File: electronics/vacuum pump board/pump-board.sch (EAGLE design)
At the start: 6 parts, among them J1 JST-PH3

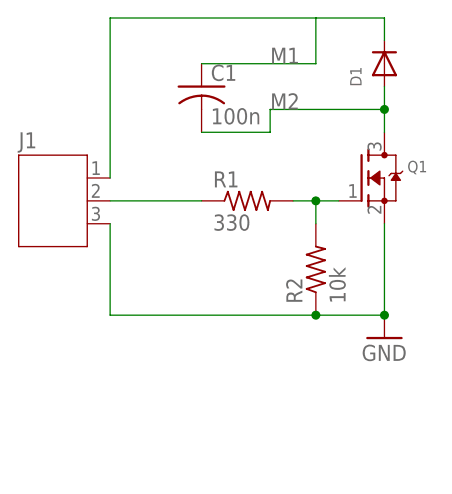
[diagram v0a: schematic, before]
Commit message: updated all PCBs and added PDF schematics
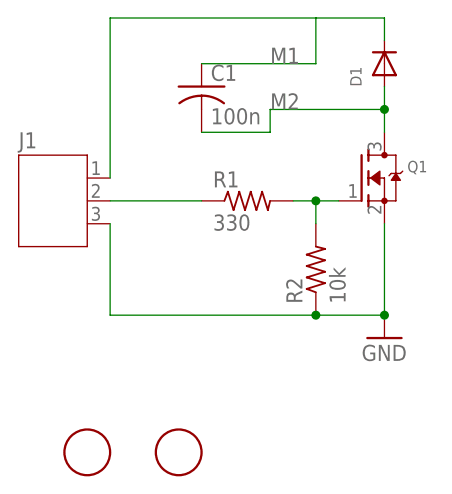
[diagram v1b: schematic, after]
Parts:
- added U$1, U$2: FIDUCIAL, adafruit:FIDUCIAL
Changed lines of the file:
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@@
 <grid distance="0.1" unitdist="inch" unit="inch" style="lines" multiple="1" display="yes" altdistance="0.01" altunitdist="inch" altunit="inch"/>
 <layers>
-<layer number="1" name="Top" color="4" fill="1" visible="yes" active="no"/>
-<layer number="2" name="Route2" color="1" fill="3" visible="yes" active="no"/>
-<layer number="3" name="Route3" color="4" fill="3" visible="yes" active="no"/>
-<layer number="4" name="Route4" color="1" fill="4" visible="yes" active="no"/>
-<layer number="5" name="Route5" color="4" fill="4" visible="yes" active="no"/>
-<layer number="6" name="Route6" color="1" fill="8" visible="yes" active="no"/>
-<layer number="7" name="Route7" color="4" fill="8" visible="yes" active="no"/>
-<layer number="8" name="Route8" color="1" fill="2" visible="yes" active="no"/>
-<layer number="9" name="Route9" color="4" fill="2" visible="yes" active="no"/>
-<layer number="10" name="Route10" color="1" fill="7" visible="yes" active="no"/>
-<layer number="11" name="Route11" color="4" fill="7" visible="yes" active="no"/>
-<layer number="12" name="Route12" color="1" fill="5" visible="yes" active="no"/>
-<layer number="13" name="Route13" color="4" fill="5" visible="yes" active="no"/>
-<layer number="14" name="Route14" color="1" fill="6" visible="yes" active="no"/>
-<layer number="15" name="Route15" color="4" fill="6" visible="yes" active="no"/>
-<layer number="16" name="Bottom" color="1" fill="1" visible="yes" active="no"/>
-<layer number="17" name="Pads" color="2" fill="1" visible="yes" active="no"/>
-<layer number="18" name="Vias" color="2" fill="1" visible="yes" active="no"/>
-<layer number="19" name="Unrouted" color="6" fill="1" visible="yes" active="no"/>
-<layer number="20" name="Dimension" color="15" fill="1" visible="yes" active="no"/>
-<layer number="21" name="tPlace" color="7" fill="1" visible="yes" active="no"/>
-<layer number="22" name="bPlace" color="7" fill="1" visible="yes" active="no"/>
-<layer number="23" name="tOrigins" color="15" fill="1" visible="yes" active="no"/>
-<layer number="24" name="bOrigins" color="15" fill="1" visible="yes" active="no"/>
-<layer number="25" name="tNames" color="7" fill="1" visible="yes" active="no"/>
-<layer number="26" name="bNames" color="7" fill="1" visible="yes" active="no"/>
-<layer number="27" name="tValues" color="7" fill="1" visible="yes" active="no"/>
-<layer number="28" name="bValues" color="7" fill="1" visible="yes" active="no"/>
+<layer number="1" name="Top" color="4" fill="1" visible="no" active="no"/>
+<layer number="2" name="Route2" color="1" fill="3" visible="no" active="no"/>
+<layer number="3" name="Route3" color="4" fill="3" visible="no" active="no"/>
+<layer number="4" name="Route4" color="1" fill="4" visible="no" active="no"/>
+<layer number="5" name="Route5" color="4" fill="4" visible="no" active="no"/>
+<layer number="6" name="Route6" color="1" fill="8" visible="no" active="no"/>
+<layer number="7" name="Route7" color="4" fill="8" visible="no" active="no"/>
+<layer number="8" name="Route8" color="1" fill="2" visible="no" active="no"/>
+<layer number="9" name="Route9" color="4" fill="2" visible="no" active="no"/>
+<layer number="10" name="Route10" color="1" fill="7" visible="no" active="no"/>
+<layer number="11" name="Route11" color="4" fill="7" visible="no" active="no"/>
+<layer number="12" name="Route12" color="1" fill="5" visible="no" active="no"/>
+<layer number="13" name="Route13" color="4" fill="5" visible="no" active="no"/>
+<layer number="14" name="Route14" color="1" fill="6" visible="no" active="no"/>
+<layer number="15" name="Route15" color="4" fill="6" visible="no" active="no"/>
+<layer number="16" name="Bottom" color="1" fill="1" visible="no" active="no"/>
+<layer number="17" name="Pads" color="2" fill="1" visible="no" active="no"/>
+<layer number="18" name="Vias" color="2" fill="1" visible="no" active="no"/>
+<layer number="19" name="Unrouted" color="6" fill="1" visible="no" active="no"/>
+<layer number="20" name="Dimension" color="15" fill="1" visible="no" active="no"/>
+<layer number="21" name="tPlace" color="7" fill="1" visible="no" active="no"/>
+<layer number="22" name="bPlace" color="7" fill="1" visible="no" active="no"/>
+<layer number="23" name="tOrigins" color="15" fill="1" visible="no" active="no"/>
+<layer number="24" name="bOrigins" color="15" fill="1" visible="no" active="no"/>
+<layer number="25" name="tNames" color="7" fill="1" visible="no" active="no"/>
+<layer number="26" name="bNames" color="7" fill="1" visible="no" active="no"/>
+<layer number="27" name="tValues" color="7" fill="1" visible="no" active="no"/>
+<layer number="28" name="bValues" color="7" fill="1" visible="no" active="no"/>
 <layer number="29" name="tStop" color="7" fill="3" visible="no" active="no"/>
 <layer number="30" name="bStop" color="7" fill="6" visible="no" active="no"/>
@@
 <layer number="35" name="tGlue" color="7" fill="4" visible="no" active="no"/>
 <layer number="36" name="bGlue" color="7" fill="5" visible="no" active="no"/>
-<layer number="37" name="tTest" color="7" fill="1" visible="yes" active="no"/>
-<layer number="38" name="bTest" color="7" fill="1" visible="yes" active="no"/>
+<layer number="37" name="tTest" color="7" fill="1" visible="no" active="no"/>
+<layer number="38" name="bTest" color="7" fill="1" visible="no" active="no"/>
 <layer number="39" name="tKeepout" color="4" fill="11" visible="no" active="no"/>
 <layer number="40" name="bKeepout" color="1" fill="11" visible="no" active="no"/>
@@
 <layer number="44" name="Drills" color="7" fill="1" visible="no" active="no"/>
 <layer number="45" name="Holes" color="7" fill="1" visible="no" active="no"/>
-<layer number="46" name="Milling" color="3" fill="1" visible="yes" active="no"/>
-<layer number="47" name="Measures" color="7" fill="1" visible="yes" active="no"/>
-<layer number="48" name="Document" color="7" fill="1" visible="yes" active="no"/>
-<layer number="49" name="Reference" color="7" fill="1" visible="yes" active="no"/>
-<layer number="50" name="dxf" color="7" fill="1" visible="yes" active="no"/>
-<layer number="51" name="tDocu" color="7" fill="1" visible="yes" active="no"/>
-<layer number="52" name="bDocu" color="7" fill="1" visible="yes" active="no"/>
-<layer number="53" name="tGND_GNDA" color="7" fill="9" visible="yes" active="no"/>
-<layer number="54" name="bGND_GNDA" color="1" fill="9" visible="yes" active="no"/>
-<layer number="56" name="wert" color="7" fill="1" visible="yes" active="no"/>
-<layer number="57" name="tCAD" color="7" fill="1" visible="yes" active="no"/>
+<layer number="46" name="Milling" color="3" fill="1" visible="no" active="no"/>
+<layer number="47" name="Measures" color="7" fill="1" visible="no" active="no"/>
+<layer number="48" name="Document" color="7" fill="1" visible="no" active="no"/>
+<layer number="49" name="Reference" color="7" fill="1" visible="no" active="no"/>
+<layer number="50" name="dxf" color="7" fill="1" visible="no" active="no"/>
+<layer number="51" name="tDocu" color="7" fill="1" visible="no" active="no"/>
+<layer number="52" name="bDocu" color="7" fill="1" visible="no" active="no"/>
+<layer number="53" name="tGND_GNDA" color="7" fill="9" visible="no" active="no"/>
+<layer number="54" name="bGND_GNDA" color="1" fill="9" visible="no" active="no"/>
+<layer number="56" name="wert" color="7" fill="1" visible="no" active="no"/>
+<layer number="57" name="tCAD" color="7" fill="1" visible="no" active="no"/>
 <layer number="90" name="Modules" color="5" fill="1" visible="no" active="yes"/>
 <layer number="91" name="Nets" color="2" fill="1" visible="yes" active="yes"/>
@@
 <part name="R2" library="adafruit" deviceset="R-US_" device="R1206" value="10k"/>
 <part name="C1" library="adafruit" deviceset="C-US" device="C1206" value="100n"/>
+<part name="U$1" library="adafruit" deviceset="FIDUCIAL" device=""/>
+<part name="U$2" library="adafruit" deviceset="FIDUCIAL" device=""/>
 </parts>
 <sheets>
@@
 <instance part="R2" gate="G$1" x="30.48" y="33.02" rot="R90"/>
 <instance part="C1" gate="G$1" x="17.78" y="53.34"/>
+<instance part="U$1" gate="G$1" x="5.08" y="12.7"/>
+<instance part="U$2" gate="G$1" x="15.24" y="12.7"/>
 </instances>
 <busses>
